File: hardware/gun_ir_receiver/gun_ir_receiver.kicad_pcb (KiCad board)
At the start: 2 copper layers, 25 x 25 mm, 3 parts

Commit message: Added gerber files
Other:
- board size 25 x 25 mm -> 19.7 x 17.8 mm
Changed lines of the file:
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@@
   (general
     (thickness 1.6)
-    (drawings 2)
+    (drawings 5)
     (tracks 13)
     (zones 0)
@@
     (pad_to_mask_clearance 0.051)
     (solder_mask_min_width 0.25)
-    (aux_axis_origin 111.125 114.3)
+    (aux_axis_origin 110.49 115.57)
     (visible_elements FFFFFF7F)
     (pcbplotparams
-      (layerselection 0x010fc_ffffffff)
+      (layerselection 0x01000_7fffffff)
       (usegerberextensions false)
       (usegerberattributes false)
@@
       (viasonmask false)
       (mode 1)
-      (useauxorigin false)
+      (useauxorigin true)
       (hpglpennumber 1)
       (hpglpenspeed 20)
@@
       (outputformat 1)
       (mirror false)
-      (drillshape 1)
+      (drillshape 0)
       (scaleselection 1)
-      (outputdirectory ""))
+      (outputdirectory "gerber/"))
   )
   (net 0 "")
@@
     )
   )
+  (gr_line (start 111.125 114.3) (end 111.125 96.52) (layer Edge.Cuts) (width 0.15))
+  (gr_line (start 130.81 114.3) (end 111.125 114.3) (layer Edge.Cuts) (width 0.15))
+  (gr_line (start 130.81 96.52) (end 130.81 114.3) (layer Edge.Cuts) (width 0.15))
+  (gr_line (start 111.125 96.52) (end 130.81 96.52) (layer Edge.Cuts) (width 0.15))
   (dimension 19.812 (width 0.3) (layer Dwgs.User)
     (gr_text "19,812 mm" (at 120.904 91.372) (layer Dwgs.User)
@@
     (arrow2b (pts (xy 110.998 93.472) (xy 112.124504 92.885579)))
   )
-  (gr_circle (center 120.65 105.41) (end 133.15 105.41) (layer Edge.Cuts) (width 0.15))
   (segment (start 114.622704 102.87) (end 114.3 102.547296) (width 1) (layer F.Cu) (net 1))
   (segment (start 127 102.87) (end 114.622704 102.87) (width 1) (layer F.Cu) (net 1))

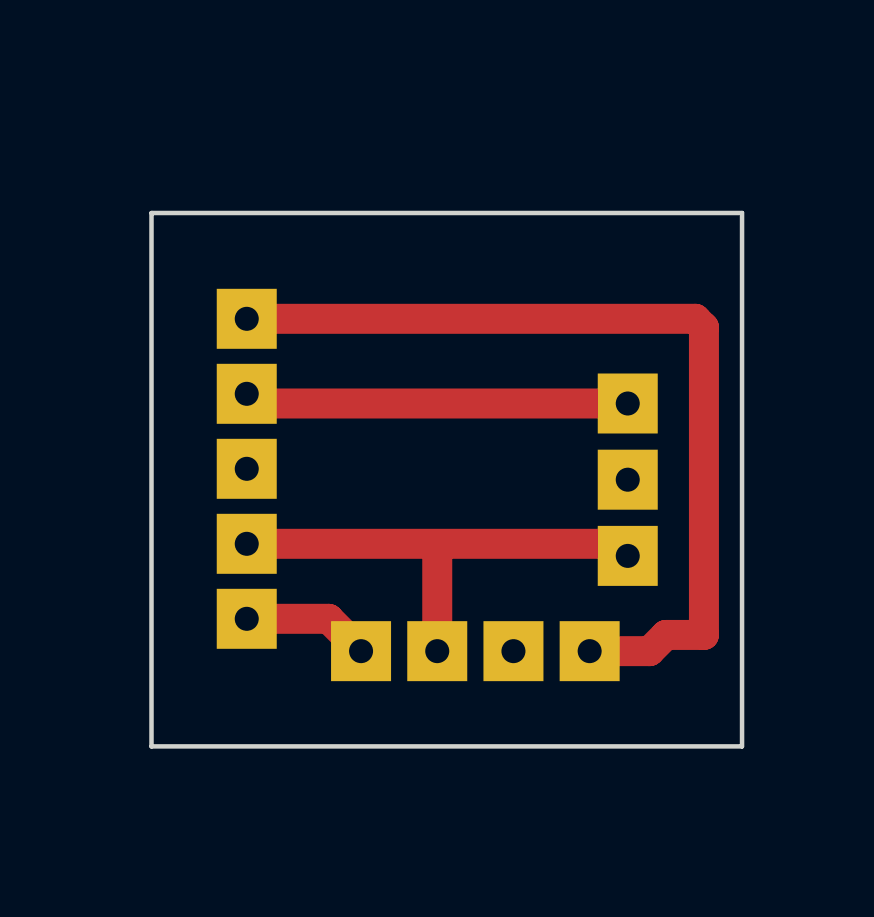
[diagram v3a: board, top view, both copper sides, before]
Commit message: Add screw holes to ir receiver pcb
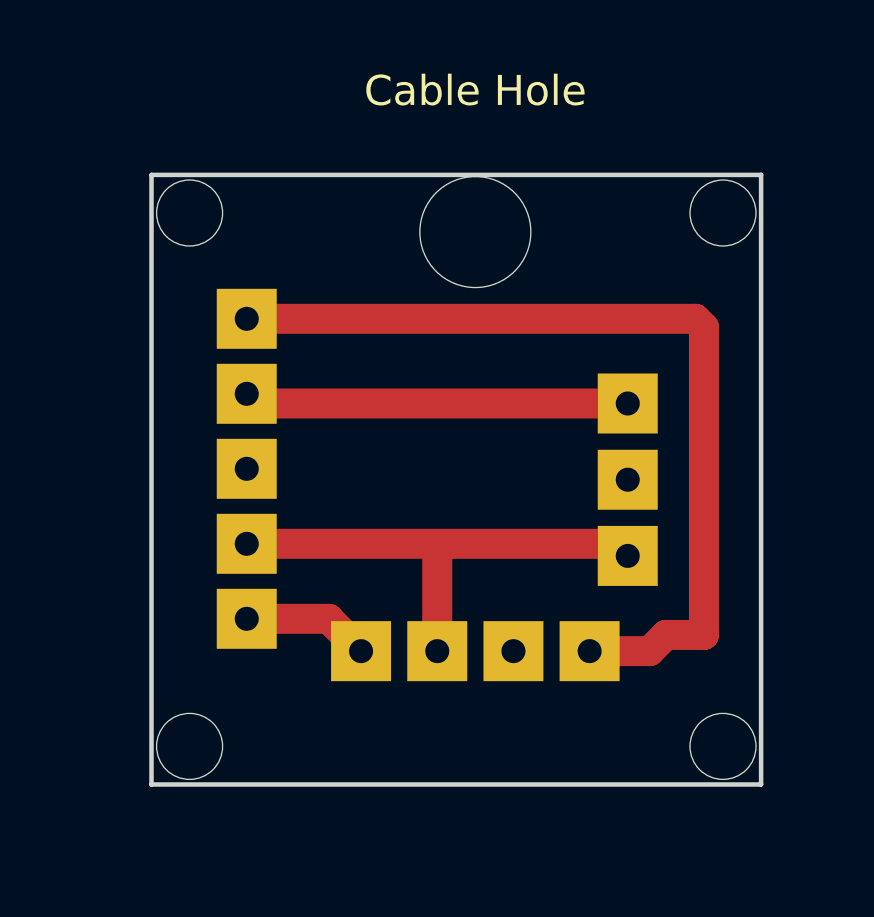
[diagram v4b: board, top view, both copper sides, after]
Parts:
- added Cable Hole: MountingHole_3.7mm, MountingHole:MountingHole_3.7mm, F.Cu at (121.9, 97.2)
- added M2: MountingHole_2.2mm_M2, MountingHole:MountingHole_2.2mm_M2, F.Cu at (112.4, 96.5)
- added M2: MountingHole_2.2mm_M2, MountingHole:MountingHole_2.2mm_M2, F.Cu at (130.2, 96.5)
- added REF**: MountingHole_2.2mm_M2, MountingHole:MountingHole_2.2mm_M2, F.Cu at (112.4, 114.3)
- added REF**: MountingHole_2.2mm_M2, MountingHole:MountingHole_2.2mm_M2, F.Cu at (130.2, 114.3)
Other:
- board size 19.7 x 17.8 mm -> 20.3 x 20.3 mm
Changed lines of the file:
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@@
-(kicad_pcb (version 20171130) (host pcbnew 5.0.1-33cea8e~68~ubuntu18.10.1)
+(kicad_pcb (version 20171130) (host pcbnew 5.0.2-bee76a0~70~ubuntu18.10.1)
   (general
     (thickness 1.6)
-    (drawings 5)
+    (drawings 6)
     (tracks 13)
     (zones 0)
-    (modules 3)
+    (modules 8)
     (nets 6)
   )
@@
     (mod_text_size 1 1)
     (mod_text_width 0.15)
-    (pad_size 2 2)
-    (pad_drill 0.8)
+    (pad_size 2.2 2.2)
+    (pad_drill 2.2)
     (pad_to_mask_clearance 0.051)
     (solder_mask_min_width 0.25)
-    (aux_axis_origin 110.49 115.57)
+    (aux_axis_origin 111.125 115.57)
     (visible_elements FFFFFF7F)
     (pcbplotparams
@@
     )
   )
-  (gr_line (start 111.125 114.3) (end 111.125 96.52) (layer Edge.Cuts) (width 0.15))
-  (gr_line (start 130.81 114.3) (end 111.125 114.3) (layer Edge.Cuts) (width 0.15))
-  (gr_line (start 130.81 96.52) (end 130.81 114.3) (layer Edge.Cuts) (width 0.15))
-  (gr_line (start 111.125 96.52) (end 130.81 96.52) (layer Edge.Cuts) (width 0.15))
-  (dimension 19.812 (width 0.3) (layer Dwgs.User)
-    (gr_text "19,812 mm" (at 120.904 91.372) (layer Dwgs.User)
+  (module MountingHole:MountingHole_2.2mm_M2 (layer F.Cu)
+    (at 112.395 96.52)
+    (descr "Mounting Hole 2.2mm, no annular, M2")
+    (tags "mounting hole 2.2mm no annular m2")
+    (attr virtual)
+    (fp_text reference M2 (at 0 -3.2) (layer F.SilkS) hide
+      (effects (font (size 1 1) (thickness 0.15)))
+    )
+    (fp_text value MountingHole_2.2mm_M2 (at 0 3.2) (layer F.Fab) hide
+      (effects (font (size 1 1) (thickness 0.15)))
+    )
+    (fp_circle (center 0 0) (end 2.45 0) (layer F.CrtYd) (width 0.05))
+    (fp_circle (center 0 0) (end 2.2 0) (layer Cmts.User) (width 0.15))
+    (fp_text user %R (at 0.3 0) (layer F.Fab)
+      (effects (font (size 1 1) (thickness 0.15)))
+    )
+    (pad "" np_thru_hole circle (at 0 0) (size 2.2 2.2) (drill 2.2) (layers *.Cu *.Mask))
+  )
+  (module MountingHole:MountingHole_2.2mm_M2 (layer F.Cu)
+    (at 112.395 114.3)
+    (descr "Mounting Hole 2.2mm, no annular, M2")
+    (tags "mounting hole 2.2mm no annular m2")
+    (attr virtual)
+    (fp_text reference REF** (at 0 -3.2) (layer F.SilkS) hide
+      (effects (font (size 1 1) (thickness 0.15)))
+    )
+    (fp_text value MountingHole_2.2mm_M2 (at 0 3.2) (layer F.Fab) hide
+      (effects (font (size 1 1) (thickness 0.15)))
+    )
+    (fp_circle (center 0 0) (end 2.45 0) (layer F.CrtYd) (width 0.05))
+    (fp_circle (center 0 0) (end 2.2 0) (layer Cmts.User) (width 0.15))
+    (fp_text user %R (at 0.3 0) (layer F.Fab)
+      (effects (font (size 1 1) (thickness 0.15)))
+    )
+    (pad 1 np_thru_hole circle (at 0 0) (size 2.2 2.2) (drill 2.2) (layers *.Cu *.Mask))
+  )
+  (module MountingHole:MountingHole_2.2mm_M2 (layer F.Cu)
+    (at 130.175 114.3)
+    (descr "Mounting Hole 2.2mm, no annular, M2")
+    (tags "mounting hole 2.2mm no annular m2")
+    (attr virtual)
+    (fp_text reference REF** (at 0 -3.2) (layer F.SilkS) hide
+      (effects (font (size 1 1) (thickness 0.15)))
+    )
+    (fp_text value MountingHole_2.2mm_M2 (at 0 3.2) (layer F.Fab) hide
+      (effects (font (size 1 1) (thickness 0.15)))
+    )
+    (fp_circle (center 0 0) (end 2.45 0) (layer F.CrtYd) (width 0.05))
+    (fp_circle (center 0 0) (end 2.2 0) (layer Cmts.User) (width 0.15))
+    (fp_text user %R (at 0.3 0) (layer F.Fab)
+      (effects (font (size 1 1) (thickness 0.15)))
+    )
+    (pad 1 np_thru_hole circle (at 0 0) (size 2.2 2.2) (drill 2.2) (layers *.Cu *.Mask))
+  )
+  (module MountingHole:MountingHole_2.2mm_M2 (layer F.Cu)
+    (at 130.175 96.52)
+    (descr "Mounting Hole 2.2mm, no annular, M2")
+    (tags "mounting hole 2.2mm no annular m2")
+    (attr virtual)
+    (fp_text reference M2 (at 0 -3.2) (layer F.SilkS) hide
+      (effects (font (size 1 1) (thickness 0.15)))
+    )
+    (fp_text value MountingHole_2.2mm_M2 (at 0 3.2) (layer F.Fab) hide
+      (effects (font (size 1 1) (thickness 0.15)))
+    )
+    (fp_circle (center 0 0) (end 2.45 0) (layer F.CrtYd) (width 0.05))
+    (fp_circle (center 0 0) (end 2.2 0) (layer Cmts.User) (width 0.15))
+    (fp_text user %R (at 0.3 0) (layer F.Fab)
+      (effects (font (size 1 1) (thickness 0.15)))
+    )
+    (pad 1 np_thru_hole circle (at 0 0) (size 2.2 2.2) (drill 2.2) (layers *.Cu *.Mask))
+  )
+  (module MountingHole:MountingHole_3.7mm (layer F.Cu)
+    (at 121.92 97.155)
+    (descr "Mounting Hole 3.7mm, no annular")
+    (tags "mounting hole 3.7mm no annular")
+    (attr virtual)
+    (fp_text reference "Cable Hole" (at 0 -4.7) (layer F.SilkS)
+      (effects (font (size 1 1) (thickness 0.15)))
+    )
+    (fp_text value MountingHole_3.7mm (at 0 4.7) (layer F.Fab)
+      (effects (font (size 1 1) (thickness 0.15)))
+    )
+    (fp_circle (center 0 0) (end 3.95 0) (layer F.CrtYd) (width 0.05))
+    (fp_circle (center 0 0) (end 3.7 0) (layer Cmts.User) (width 0.15))
+    (fp_text user %R (at 0.3 0) (layer F.Fab) hide
+      (effects (font (size 1 1) (thickness 0.15)))
+    )
+    (pad 1 np_thru_hole circle (at 0 0) (size 3.7 3.7) (drill 3.7) (layers *.Cu *.Mask))
+  )
+  (dimension 20.32 (width 0.3) (layer Dwgs.User)
+    (gr_text "20,320 mm" (at 139.26 105.41 270) (layer Dwgs.User)
       (effects (font (size 1.5 1.5) (thickness 0.3)))
     )
-    (feature1 (pts (xy 130.81 95.504) (xy 130.81 92.885579)))
-    (feature2 (pts (xy 110.998 95.504) (xy 110.998 92.885579)))
-    (crossbar (pts (xy 110.998 93.472) (xy 130.81 93.472)))
-    (arrow1a (pts (xy 130.81 93.472) (xy 129.683496 94.058421)))
-    (arrow1b (pts (xy 130.81 93.472) (xy 129.683496 92.885579)))
-    (arrow2a (pts (xy 110.998 93.472) (xy 112.124504 94.058421)))
-    (arrow2b (pts (xy 110.998 93.472) (xy 112.124504 92.885579)))
-  )
+    (feature1 (pts (xy 131.445 115.57) (xy 137.746421 115.57)))
+    (feature2 (pts (xy 131.445 95.25) (xy 137.746421 95.25)))
+    (crossbar (pts (xy 137.16 95.25) (xy 137.16 115.57)))
+    (arrow1a (pts (xy 137.16 115.57) (xy 136.573579 114.443496)))
+    (arrow1b (pts (xy 137.16 115.57) (xy 137.746421 114.443496)))
+    (arrow2a (pts (xy 137.16 95.25) (xy 136.573579 96.376504)))
+    (arrow2b (pts (xy 137.16 95.25) (xy 137.746421 96.376504)))
+  )
+  (dimension 20.32 (width 0.3) (layer Dwgs.User)
+    (gr_text "20,320 mm" (at 121.285 85.53) (layer Dwgs.User)
+      (effects (font (size 1.5 1.5) (thickness 0.3)))
+    )
+    (feature1 (pts (xy 131.445 95.25) (xy 131.445 87.043579)))
+    (feature2 (pts (xy 111.125 95.25) (xy 111.125 87.043579)))
+    (crossbar (pts (xy 111.125 87.63) (xy 131.445 87.63)))
+    (arrow1a (pts (xy 131.445 87.63) (xy 130.318496 88.216421)))
+    (arrow1b (pts (xy 131.445 87.63) (xy 130.318496 87.043579)))
+    (arrow2a (pts (xy 111.125 87.63) (xy 112.251504 88.216421)))
+    (arrow2b (pts (xy 111.125 87.63) (xy 112.251504 87.043579)))
+  )
+  (gr_line (start 111.125 95.25) (end 111.125 115.57) (layer Edge.Cuts) (width 0.15))
+  (gr_line (start 131.445 95.25) (end 111.125 95.25) (layer Edge.Cuts) (width 0.15))
+  (gr_line (start 131.445 115.57) (end 131.445 95.25) (layer Edge.Cuts) (width 0.15))
+  (gr_line (start 111.125 115.57) (end 131.445 115.57) (layer Edge.Cuts) (width 0.15))
   (segment (start 114.622704 102.87) (end 114.3 102.547296) (width 1) (layer F.Cu) (net 1))
   (segment (start 127 102.87) (end 114.622704 102.87) (width 1) (layer F.Cu) (net 1))
@@
     (polygon
       (pts
-        (xy 111.125 114.3) (xy 130.81 114.3) (xy 130.81 96.52) (xy 111.125 96.52)
+        (xy 111.125 115.57) (xy 131.445 115.57) (xy 131.445 95.25) (xy 111.125 95.25)
       )
     )
